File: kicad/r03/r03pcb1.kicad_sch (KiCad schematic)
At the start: 7 parts, among them J1 Conn_01x08_Pin, Q1 NMOS, U1 BL-128HR01A

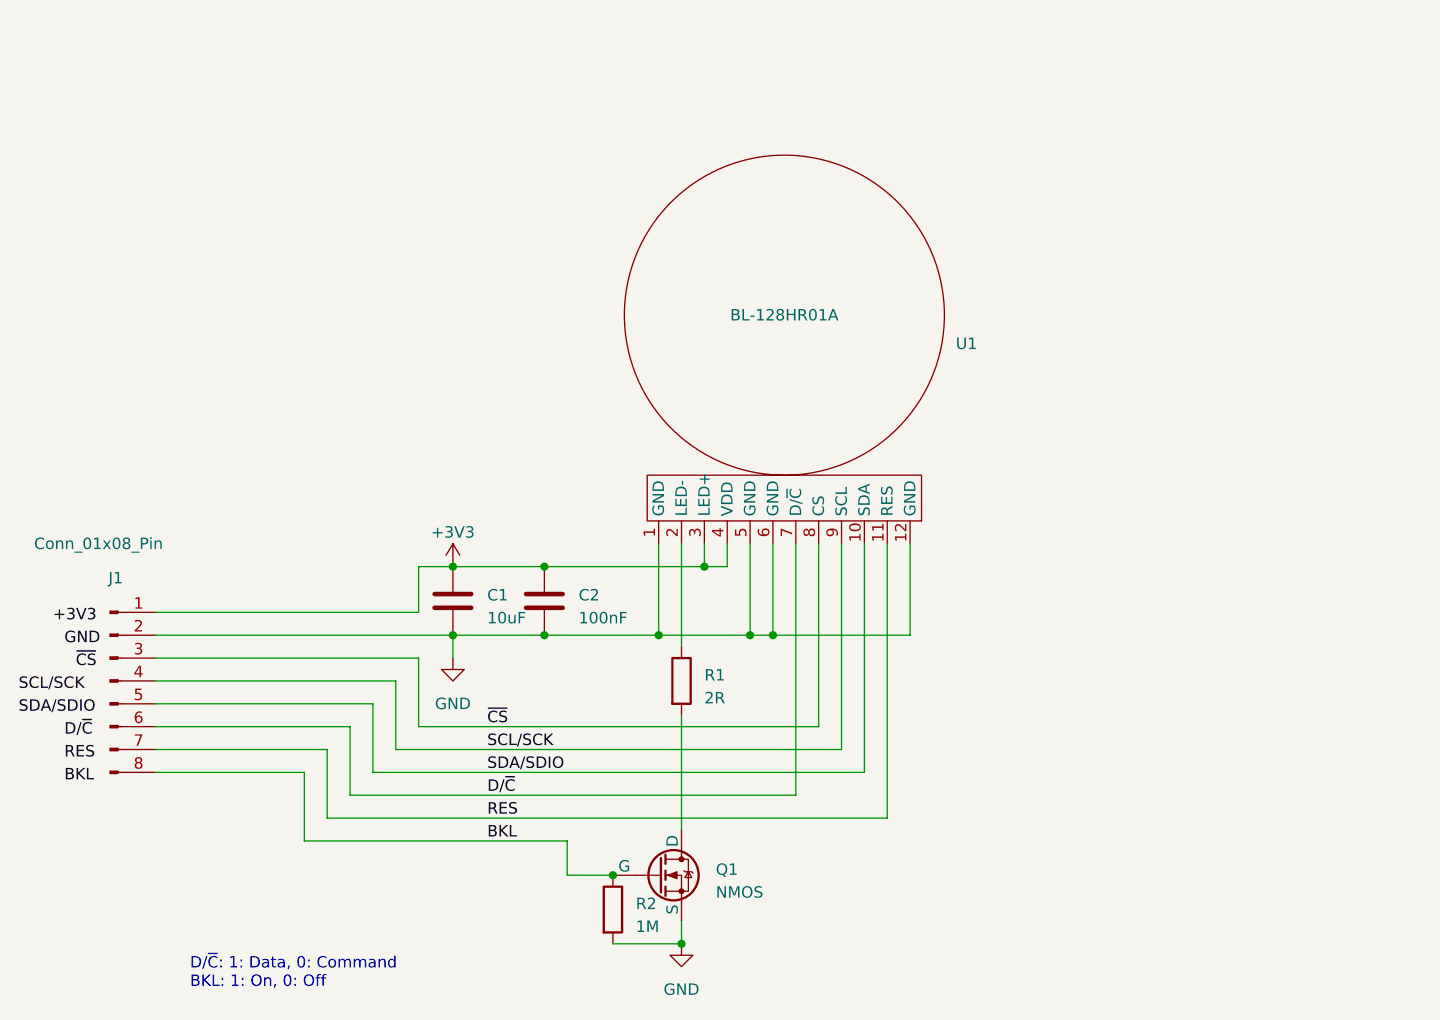
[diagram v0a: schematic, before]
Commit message: r03: started mcu pcb (pcb2), deleted r01
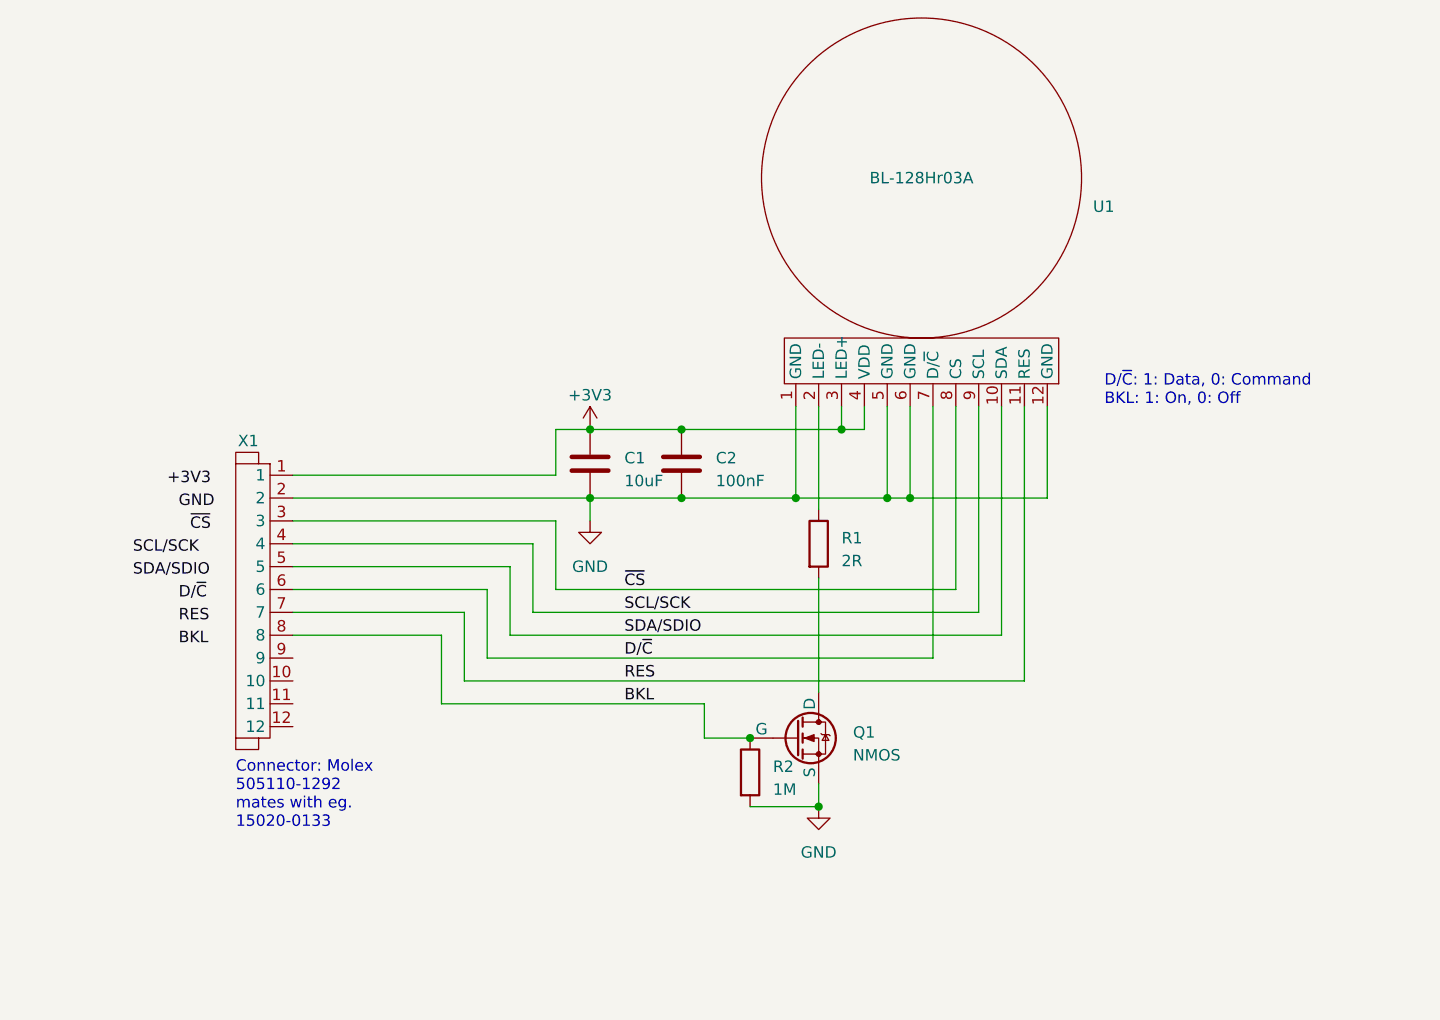
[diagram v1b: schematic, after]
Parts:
- removed J1: Conn_01x08_Pin, symbol Connector:Conn_01x08_Pin
- added X1: ~, MEgli:505110-1292, symbol MEgli:505110-1292
- U1: value BL-128HR01A -> BL-128Hr03A
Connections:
- net +3V3: now also X1.1
- net BKL: now also X1.8
- net D/~{C}: now also X1.6
- net GND: now also X1.2
- net RES: now also X1.7
- net SCL/SCK: now also X1.4
- net SDA/SDIO: now also X1.5
- net ~{CS}: now also X1.3
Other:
- note added: "Connector: Molex 505110-1292 mates with eg. 15020-0133"
- company: (none) -> MEgliDevelopment
- title: (none) -> r03 PCB1: Display
